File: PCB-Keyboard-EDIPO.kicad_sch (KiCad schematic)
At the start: 21 parts, among them J1 AVR-ISP-6, SW68 SW_Push_Reset, U1 ATmega32U4-A, U2 PRTR5V0U2X, Y1 XTAL

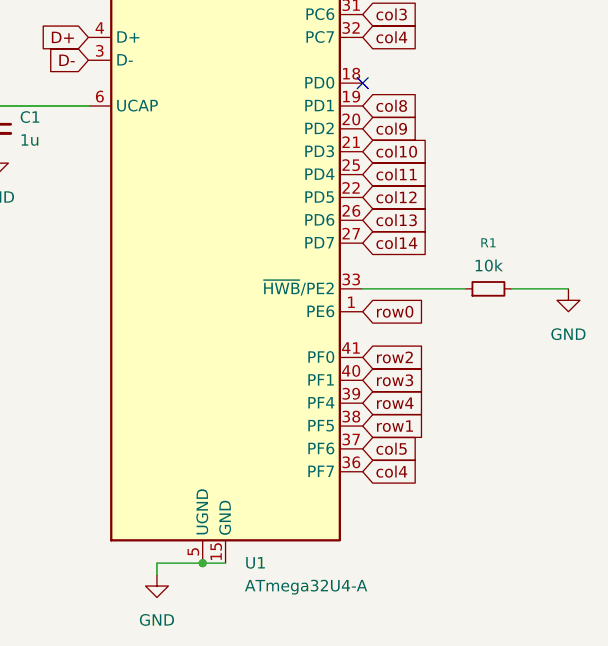
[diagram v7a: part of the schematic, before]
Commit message: Rough Routing Completed
Must now fix errors if any
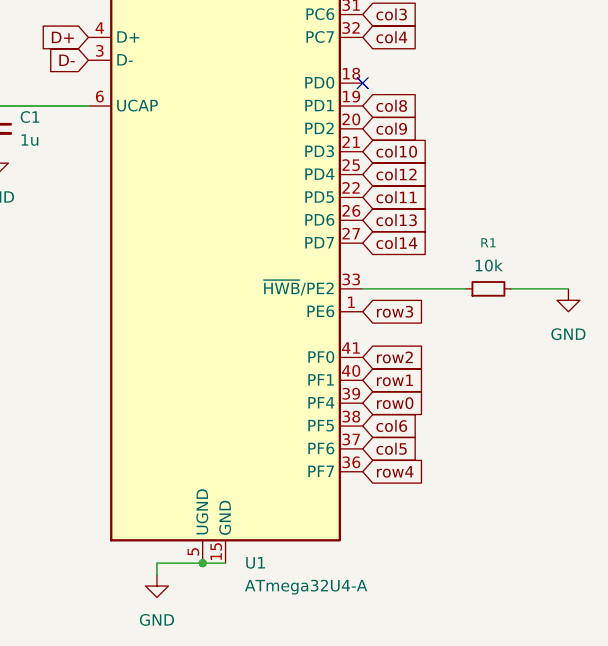
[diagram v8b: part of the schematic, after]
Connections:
- net col11: now also U1.22 (PD5); no longer U1.25 (PD4)
- net col12: now also U1.25 (PD4); no longer U1.22 (PD5)
- net col4: no longer U1.36 (PF7)
- net row0: now also U1.39 (PF4); no longer U1.1 (PE6)
- net row1: now also U1.40 (PF1); no longer U1.38 (PF5)
- net row3: now also U1.1 (PE6); no longer U1.40 (PF1)
- net row4: now also U1.36 (PF7); no longer U1.39 (PF4)
- new net col6: U1.38 (PF5)
